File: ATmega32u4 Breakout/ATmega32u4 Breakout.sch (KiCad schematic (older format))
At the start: 6 parts, among them J1 Conn_01x22_Male, J2 Conn_01x22_Male, U1 ATmega32U4-AU, Y1 16MHz

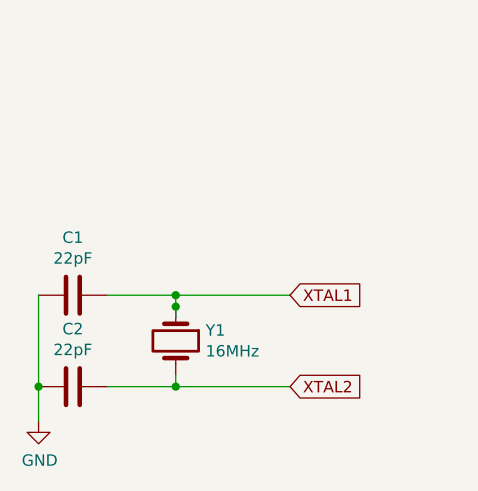
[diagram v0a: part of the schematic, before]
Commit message: Moving labels around
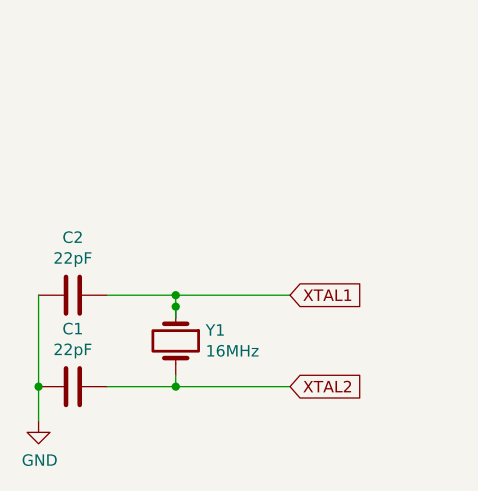
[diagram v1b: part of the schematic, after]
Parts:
- renumbered C2 to C1, C1 to C2
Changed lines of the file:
@@
 $EndComp
 $Comp
-L Device:C C1
+L Device:C C2
 U 1 1 5FA2D004
 P 2750 6050
-F 0 "C1" V 2498 6050 50  0000 C CNN
+F 0 "C2" V 2498 6050 50  0000 C CNN
 F 1 "22pF" V 2589 6050 50  0000 C CNN
 F 2 "Capacitor_THT:C_Disc_D3.0mm_W1.6mm_P2.50mm" H 2788 5900 50  0001 C CNN
@@
 $EndComp
 $Comp
-L Device:C C2
+L Device:C C1
 U 1 1 5FA2D75D
 P 2750 6450
-F 0 "C2" V 2498 6450 50  0000 C CNN
+F 0 "C1" V 2498 6450 50  0000 C CNN
 F 1 "22pF" V 2589 6450 50  0000 C CNN
 F 2 "Capacitor_THT:C_Disc_D3.0mm_W1.6mm_P2.50mm" H 2788 6300 50  0001 C CNN

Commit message: Lots of work over the weekend.
Nearly done, gerber files made too.  I think it's ready to be turned into PCB.
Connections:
- wire segments 11 -> 10
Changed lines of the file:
@@
 	1    0    0    -1
 $EndComp
-Wire Wire Line
-	6350 4200 6500 4200
-Text GLabel 6500 4200 2    50   Input ~ 0
+Text GLabel 6350 4200 2    50   Input ~ 0
 D7
 Text GLabel 3200 2500 2    50   Input ~ 0
